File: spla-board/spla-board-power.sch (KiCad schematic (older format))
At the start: 70 parts, among them J12 J_POWER, J4 J_POWER2, J7 Barrel_Jack, U14 TLV73311PDBV, U7 ST1S10PHR, U8 ST1S10PHR, U9 TLV73325PDBV

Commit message: schematic/pcb: Remove unnecessary electrolytic capacitors.
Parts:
- removed C71: NOSTUFF, Capacitor_THT:CP_Radial_D10.0mm_P5.00mm, symbol Device:CP
- removed C72: NOSTUFF, Capacitor_THT:CP_Radial_D7.5mm_P2.50mm, symbol Device:CP
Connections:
- wire segments 244 -> 237
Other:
- moved on the sheet: J7, TP6
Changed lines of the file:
@@
 L Connector:Barrel_Jack J7
 U 1 1 5E532515
-P 1050 3450
-F 0 "J7" H 1107 3775 50  0000 C CNN
-F 1 "Barrel_Jack" H 1107 3684 50  0000 C CNN
-F 2 "Connector_BarrelJack:BarrelJack_CUI_PJ-036AH-SMT_Horizontal" H 1100 3410 50  0001 C CNN
-F 3 "~" H 1100 3410 50  0001 C CNN
-F 4 "CP-036AHPJCT-ND" H 1050 3450 50  0001 C CNN "Digikey"
-F 5 "PJ-036AH-SMT-TR" H 1050 3450 50  0001 C CNN "Manufacturer Id"
-F 6 "CUI Devices" H 1050 3450 50  0001 C CNN "Manufacturer"
-	1    1050 3450
-	1    0    0    -1
-$EndComp
-Wire Wire Line
-	1350 3550 1450 3550
-Wire Wire Line
-	1350 3350 1450 3350
-Wire Wire Line
-	1450 3350 1450 3250
+P 1600 3450
+F 0 "J7" H 1657 3775 50  0000 C CNN
+F 1 "Barrel_Jack" H 1657 3684 50  0000 C CNN
+F 2 "Connector_BarrelJack:BarrelJack_CUI_PJ-036AH-SMT_Horizontal" H 1650 3410 50  0001 C CNN
+F 3 "~" H 1650 3410 50  0001 C CNN
+F 4 "CP-036AHPJCT-ND" H 1600 3450 50  0001 C CNN "Digikey"
+F 5 "PJ-036AH-SMT-TR" H 1600 3450 50  0001 C CNN "Manufacturer Id"
+F 6 "CUI Devices" H 1600 3450 50  0001 C CNN "Manufacturer"
+	1    1600 3450
+	1    0    0    -1
+$EndComp
+Wire Wire Line
+	1900 3550 2000 3550
 $Comp
 L power:+12V #PWR029
 U 1 1 5E534EED
-P 1450 3250
-F 0 "#PWR029" H 1450 3100 50  0001 C CNN
-F 1 "+12V" H 1465 3423 50  0000 C CNN
-F 2 "" H 1450 3250 50  0001 C CNN
-F 3 "" H 1450 3250 50  0001 C CNN
-	1    1450 3250
-	1    0    0    -1
-$EndComp
-Wire Wire Line
-	1450 3350 1750 3350
-Connection ~ 1450 3350
+P 3400 3200
+F 0 "#PWR029" H 3400 3050 50  0001 C CNN
+F 1 "+12V" H 3415 3373 50  0000 C CNN
+F 2 "" H 3400 3200 50  0001 C CNN
+F 3 "" H 3400 3200 50  0001 C CNN
+	1    3400 3200
+	1    0    0    -1
+$EndComp
 $Comp
 L power:+5V #PWR041
@@
 L power:PWR_FLAG #FLG0101
 U 1 1 5F9445F5
-P 2050 3350
-F 0 "#FLG0101" H 2050 3425 50  0001 C CNN
-F 1 "PWR_FLAG" H 2050 3523 50  0000 C CNN
-F 2 "" H 2050 3350 50  0001 C CNN
-F 3 "~" H 2050 3350 50  0001 C CNN
-	1    2050 3350
+P 2450 3350
+F 0 "#FLG0101" H 2450 3425 50  0001 C CNN
+F 1 "PWR_FLAG" H 2450 3523 50  0000 C CNN
+F 2 "" H 2450 3350 50  0001 C CNN
+F 3 "~" H 2450 3350 50  0001 C CNN
+	1    2450 3350
 	1    0    0    -1
 $EndComp
@@
 Text Notes 5000 4400 2    50   ~ 0
 SYNC = use internal 900kHz oscillator
-Connection ~ 2050 3350
-Wire Wire Line
-	2050 3350 2400 3350
+Connection ~ 2450 3350
 $Comp
 L Device:R_Small R87
@@
 	4100 10250 4100 10350
 Connection ~ 2850 4050
-Wire Wire Line
-	2850 4050 2400 4050
 $Comp
 L Connector:TestPoint TP6
 U 1 1 5EAFCBB1
-P 2850 4050
-F 0 "TP6" H 2908 4168 50  0000 L CNN
-F 1 "TP_GND" H 2908 4077 50  0000 L CNN
-F 2 "TestPoint:TestPoint_Pad_D2.0mm" H 3050 4050 50  0001 C CNN
-F 3 "~" H 3050 4050 50  0001 C CNN
-F 4 "N/A" H 2850 4050 50  0001 C CNN "Digikey"
-F 5 "N/A" H 2850 4050 50  0001 C CNN "Manufacturer Id"
-F 6 "N/A" H 2850 4050 50  0001 C CNN "Manufacturer"
-	1    2850 4050
-	1    0    0    -1
-$EndComp
-Wire Wire Line
-	1450 3550 1450 4050
+P 2850 3950
+F 0 "TP6" H 2908 4068 50  0000 L CNN
+F 1 "TP_GND" H 2908 3977 50  0000 L CNN
+F 2 "TestPoint:TestPoint_Pad_D2.0mm" H 3050 3950 50  0001 C CNN
+F 3 "~" H 3050 3950 50  0001 C CNN
+F 4 "N/A" H 2850 3950 50  0001 C CNN "Digikey"
+F 5 "N/A" H 2850 3950 50  0001 C CNN "Manufacturer Id"
+F 6 "N/A" H 2850 3950 50  0001 C CNN "Manufacturer"
+	1    2850 3950
+	1    0    0    -1
+$EndComp
+Wire Wire Line
+	2000 3550 2000 4050
 $Comp
 L SPLA:BomExtra BOM?
@@
 L power:GND #PWR030
 U 1 1 5E5334D6
-P 2850 4050
-F 0 "#PWR030" H 2850 3800 50  0001 C CNN
-F 1 "GND" H 2855 3877 50  0000 C CNN
-F 2 "" H 2850 4050 50  0001 C CNN
-F 3 "" H 2850 4050 50  0001 C CNN
-	1    2850 4050
-	1    0    0    -1
-$EndComp
-$Comp
-L Device:CP C71
-U 1 1 5EE4A2E3
-P 1750 3700
-F 0 "C71" H 1868 3746 50  0000 L CNN
-F 1 "NOSTUFF" H 1868 3655 50  0000 L CNN
-F 2 "Capacitor_THT:CP_Radial_D10.0mm_P5.00mm" H 1788 3550 50  0001 C CNN
-F 3 "~" H 1750 3700 50  0001 C CNN
-F 4 "N/A" H 1750 3700 50  0001 C CNN "Digikey"
-F 5 "N/A" H 1750 3700 50  0001 C CNN "Manufacturer"
-F 6 "N/A" H 1750 3700 50  0001 C CNN "Manufacturer Id"
-	1    1750 3700
-	1    0    0    -1
-$EndComp
-$Comp
-L Device:CP C72
-U 1 1 5EE4A640
-P 2400 3700
-F 0 "C72" H 2518 3746 50  0000 L CNN
-F 1 "NOSTUFF" H 2518 3655 50  0000 L CNN
-F 2 "Capacitor_THT:CP_Radial_D7.5mm_P2.50mm" H 2438 3550 50  0001 C CNN
-F 3 "~" H 2400 3700 50  0001 C CNN
-F 4 "N/A" H 2400 3700 50  0001 C CNN "Digikey"
-F 5 "N/A" H 2400 3700 50  0001 C CNN "Manufacturer"
-F 6 "N/A" H 2400 3700 50  0001 C CNN "Manufacturer Id"
-	1    2400 3700
-	1    0    0    -1
-$EndComp
-Wire Wire Line
-	1750 3550 1750 3350
-Connection ~ 1750 3350
-Wire Wire Line
-	1750 3350 2050 3350
-Wire Wire Line
-	1750 3850 1750 4050
-Connection ~ 1750 4050
-Wire Wire Line
-	1750 4050 1450 4050
-Wire Wire Line
-	2400 3850 2400 4050
-Connection ~ 2400 4050
-Wire Wire Line
-	2400 4050 1750 4050
-Wire Wire Line
-	2400 3550 2400 3350
-Connection ~ 2400 3350
-Wire Wire Line
-	2400 3350 2850 3350
+P 2850 4150
+F 0 "#PWR030" H 2850 3900 50  0001 C CNN
+F 1 "GND" H 2855 3977 50  0000 C CNN
+F 2 "" H 2850 4150 50  0001 C CNN
+F 3 "" H 2850 4150 50  0001 C CNN
+	1    2850 4150
+	1    0    0    -1
+$EndComp
+Wire Wire Line
+	2450 3350 2850 3350
+Wire Wire Line
+	2000 4050 2850 4050
+Wire Wire Line
+	2850 3950 2850 4050
+Wire Wire Line
+	2850 4050 2850 4150
+Wire Wire Line
+	3400 3200 3400 3350
+Wire Wire Line
+	1900 3350 2450 3350
 $EndSCHEMATC

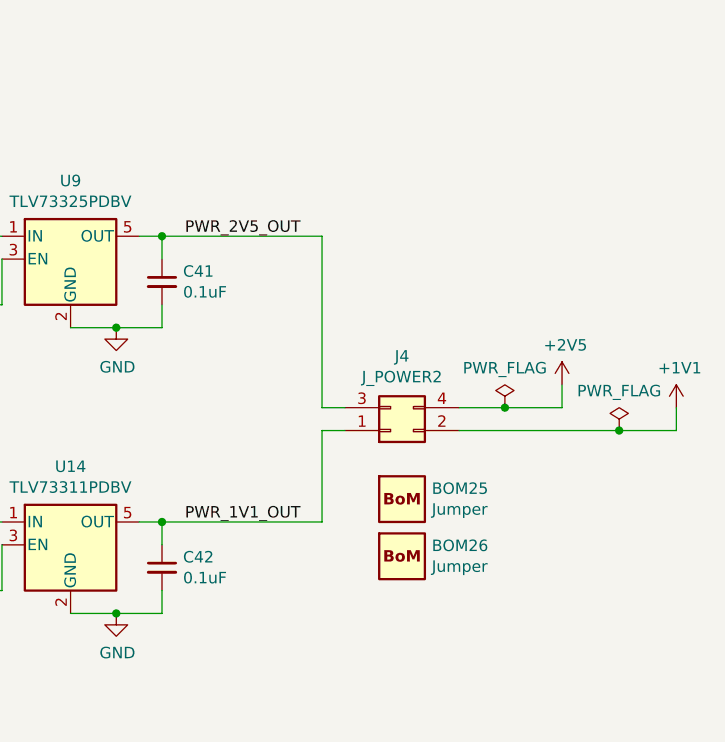
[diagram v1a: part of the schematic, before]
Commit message: schematic/pcb: Remove J4, which is unnecessary and meltable.
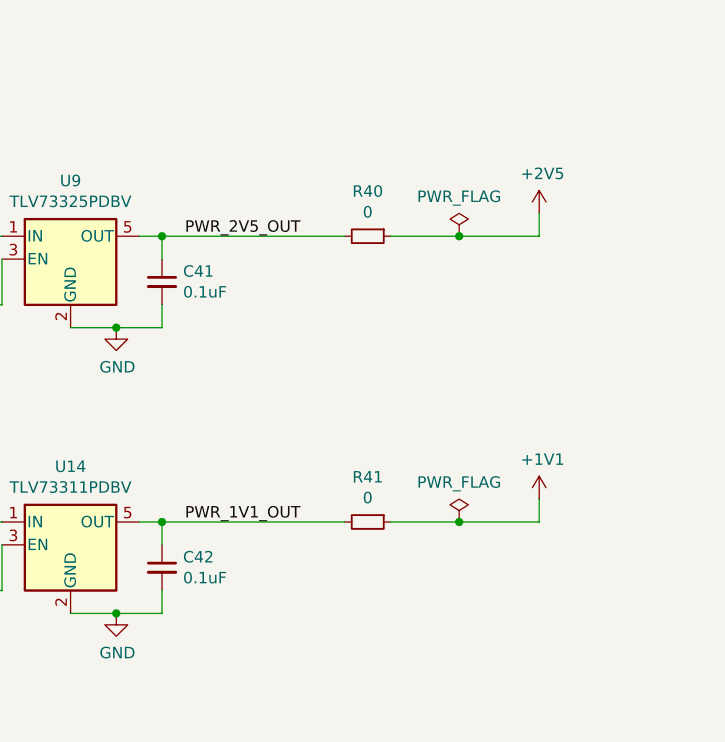
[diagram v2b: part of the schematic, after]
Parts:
- removed BOM25, BOM26: Jumper, SPLA:BoM, symbol SPLA:BomExtra
- removed J4: J_POWER2, Connector_PinHeader_2.54mm:PinHeader_2x02_P2.54mm_Vertical, symbol Connector_Generic:Conn_02x02_Odd_Even
- added R40, R41: 0, Resistor_SMD:R_0603_1608Metric, symbol Device:R_Small
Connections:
- net +1V1: now also R41.1
- net +2V5: now also R40.1
- net PWR_1V1_OUT: now also R41.2
- net PWR_2V5_OUT: now also R40.2
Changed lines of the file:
@@
 Connection ~ 12050 5100
 Wire Wire Line
-	15350 5850 15350 5750
-Wire Wire Line
-	15850 5850 15850 5950
+	15250 5100 15250 5000
+Wire Wire Line
+	15250 6250 15250 6350
 $Comp
 L power:+1V1 #PWR044
 U 1 1 5E56FFF6
-P 15850 5850
-F 0 "#PWR044" H 15850 5700 50  0001 C CNN
-F 1 "+1V1" H 15865 6023 50  0000 C CNN
-F 2 "" H 15850 5850 50  0001 C CNN
-F 3 "" H 15850 5850 50  0001 C CNN
-	1    15850 5850
+P 15250 6250
+F 0 "#PWR044" H 15250 6100 50  0001 C CNN
+F 1 "+1V1" H 15265 6423 50  0000 C CNN
+F 2 "" H 15250 6250 50  0001 C CNN
+F 3 "" H 15250 6250 50  0001 C CNN
+	1    15250 6250
 	1    0    0    -1
 $EndComp
@@
 L power:+2V5 #PWR043
 U 1 1 5E56BE1E
-P 15350 5750
-F 0 "#PWR043" H 15350 5600 50  0001 C CNN
-F 1 "+2V5" H 15365 5923 50  0000 C CNN
-F 2 "" H 15350 5750 50  0001 C CNN
-F 3 "" H 15350 5750 50  0001 C CNN
-	1    15350 5750
+P 15250 5000
+F 0 "#PWR043" H 15250 4850 50  0001 C CNN
+F 1 "+2V5" H 15265 5173 50  0000 C CNN
+F 2 "" H 15250 5000 50  0001 C CNN
+F 3 "" H 15250 5000 50  0001 C CNN
+	1    15250 5000
 	1    0    0    -1
 $EndComp
@@
 Wire Wire Line
 	11850 6350 12050 6350
-$Comp
-L Connector_Generic:Conn_02x02_Odd_Even J4
-U 1 1 5F14B7D8
-P 14600 5950
-F 0 "J4" H 14650 5625 50  0000 C CNN
-F 1 "J_POWER2" H 14650 5716 50  0000 C CNN
-F 2 "Connector_PinHeader_2.54mm:PinHeader_2x02_P2.54mm_Vertical" H 14600 5950 50  0001 C CNN
-F 3 "~" H 14600 5950 50  0001 C CNN
-F 4 "S2011EC-40-ND" H 14600 5950 50  0001 C CNN "Digikey"
-F 5 "PRPC040DAAN-RC" H 14600 5950 50  0001 C CNN "Manufacturer Id"
-F 6 "Sullins Connector Solutions" H 14600 5950 50  0001 C CNN "Manufacturer"
-	1    14600 5950
-	1    0    0    1
-$EndComp
-Wire Wire Line
-	13600 5100 14300 5100
-Wire Wire Line
-	14300 5100 14300 5850
-Wire Wire Line
-	14300 5850 14400 5850
 Connection ~ 13600 5100
-Wire Wire Line
-	14400 5950 14300 5950
-Wire Wire Line
-	14300 5950 14300 6350
-Wire Wire Line
-	14300 6350 13600 6350
 Connection ~ 13600 6350
 $Comp
 L power:PWR_FLAG #FLG0106
 U 1 1 5F180F83
-P 15100 5850
-F 0 "#FLG0106" H 15100 5925 50  0001 C CNN
-F 1 "PWR_FLAG" H 15100 6023 50  0000 C CNN
-F 2 "" H 15100 5850 50  0001 C CNN
-F 3 "~" H 15100 5850 50  0001 C CNN
-	1    15100 5850
+P 14900 5100
+F 0 "#FLG0106" H 14900 5175 50  0001 C CNN
+F 1 "PWR_FLAG" H 14900 5273 50  0000 C CNN
+F 2 "" H 14900 5100 50  0001 C CNN
+F 3 "~" H 14900 5100 50  0001 C CNN
+	1    14900 5100
 	1    0    0    -1
 $EndComp
@@
 L power:PWR_FLAG #FLG0107
 U 1 1 5F1887AE
-P 15600 5950
-F 0 "#FLG0107" H 15600 6025 50  0001 C CNN
-F 1 "PWR_FLAG" H 15600 6123 50  0000 C CNN
-F 2 "" H 15600 5950 50  0001 C CNN
-F 3 "~" H 15600 5950 50  0001 C CNN
-	1    15600 5950
-	1    0    0    -1
-$EndComp
-Wire Wire Line
-	15350 5850 15100 5850
-Connection ~ 15100 5850
-Wire Wire Line
-	15100 5850 14900 5850
-Wire Wire Line
-	14900 5950 15600 5950
-Connection ~ 15600 5950
-Wire Wire Line
-	15600 5950 15850 5950
+P 14900 6350
+F 0 "#FLG0107" H 14900 6425 50  0001 C CNN
+F 1 "PWR_FLAG" H 14900 6523 50  0000 C CNN
+F 2 "" H 14900 6350 50  0001 C CNN
+F 3 "~" H 14900 6350 50  0001 C CNN
+	1    14900 6350
+	1    0    0    -1
+$EndComp
 Text Label 13700 5100 0    50   ~ 0
 PWR_2V5_OUT
@@
 $Comp
 L SPLA:BomExtra BOM?
-U 1 1 5EC1E4A3
-P 14650 6250
-AR Path="/5E50E589/5EC1E4A3" Ref="BOM?"  Part="1"
-AR Path="/5E50D39B/5EC1E4A3" Ref="BOM25"  Part="1"
-F 0 "BOM25" H 14780 6296 50  0000 L CNN
-F 1 "Jumper" H 14780 6205 50  0000 L CNN
-F 2 "SPLA:BoM" H 14650 6250 50  0001 C CNN
-F 3 "" H 14650 6250 50  0001 C CNN
-F 4 "S9337-ND" H 14650 6250 50  0001 C CNN "Digikey"
-F 5 "QPC02SXGN-RC" H 14650 6250 50  0001 C CNN "Manufacturer Id"
-F 6 "Sullins Connector Solutions" H 14650 6250 50  0001 C CNN "Manufacturer"
-	1    14650 6250
-	1    0    0    -1
-$EndComp
-$Comp
-L SPLA:BomExtra BOM?
-U 1 1 5EC2D1EF
-P 14650 6500
-AR Path="/5E50E589/5EC2D1EF" Ref="BOM?"  Part="1"
-AR Path="/5E50D39B/5EC2D1EF" Ref="BOM26"  Part="1"
-F 0 "BOM26" H 14780 6546 50  0000 L CNN
-F 1 "Jumper" H 14780 6455 50  0000 L CNN
-F 2 "SPLA:BoM" H 14650 6500 50  0001 C CNN
-F 3 "" H 14650 6500 50  0001 C CNN
-F 4 "S9337-ND" H 14650 6500 50  0001 C CNN "Digikey"
-F 5 "QPC02SXGN-RC" H 14650 6500 50  0001 C CNN "Manufacturer Id"
-F 6 "Sullins Connector Solutions" H 14650 6500 50  0001 C CNN "Manufacturer"
-	1    14650 6500
-	1    0    0    -1
-$EndComp
-$Comp
-L SPLA:BomExtra BOM?
 U 1 1 5EC3BD64
 P 10700 5900
@@
 Wire Wire Line
 	1900 3350 2450 3350
+$Comp
+L Device:R_Small R40
+U 1 1 5FB785AC
+P 14500 5100
+F 0 "R40" V 14304 5100 50  0000 C CNN
+F 1 "0" V 14395 5100 50  0000 C CNN
+F 2 "Resistor_SMD:R_0603_1608Metric" H 14500 5100 50  0001 C CNN
+F 3 "~" H 14500 5100 50  0001 C CNN
+F 4 "2019-RK73Z1JTTDCT-ND" H 14500 5100 50  0001 C CNN "Digikey"
+F 5 "KOA Speer Electronics Inc." H 14500 5100 50  0001 C CNN "Manufacturer"
+F 6 "RK73Z1JTTD" H 14500 5100 50  0001 C CNN "Manufacturer Id"
+	1    14500 5100
+	0    1    1    0
+$EndComp
+$Comp
+L Device:R_Small R41
+U 1 1 5FB7903C
+P 14500 6350
+F 0 "R41" V 14304 6350 50  0000 C CNN
+F 1 "0" V 14395 6350 50  0000 C CNN
+F 2 "Resistor_SMD:R_0603_1608Metric" H 14500 6350 50  0001 C CNN
+F 3 "~" H 14500 6350 50  0001 C CNN
+F 4 "2019-RK73Z1JTTDCT-ND" H 14500 6350 50  0001 C CNN "Digikey"
+F 5 "KOA Speer Electronics Inc." H 14500 6350 50  0001 C CNN "Manufacturer"
+F 6 "RK73Z1JTTD" H 14500 6350 50  0001 C CNN "Manufacturer Id"
+	1    14500 6350
+	0    1    1    0
+$EndComp
+Wire Wire Line
+	13600 5100 14400 5100
+Wire Wire Line
+	14600 5100 14900 5100
+Wire Wire Line
+	14900 6350 14600 6350
+Wire Wire Line
+	13600 6350 14400 6350
+Wire Wire Line
+	14900 5100 15250 5100
+Connection ~ 14900 5100
+Wire Wire Line
+	14900 6350 15250 6350
+Connection ~ 14900 6350
 $EndSCHEMATC

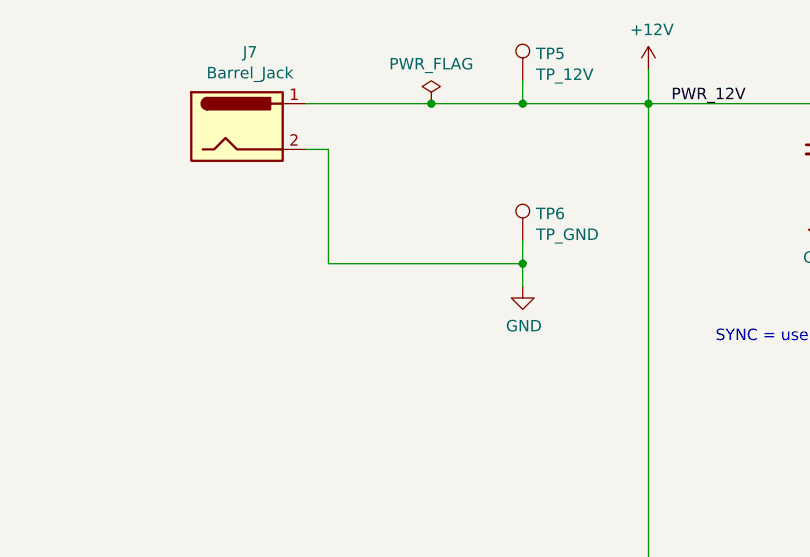
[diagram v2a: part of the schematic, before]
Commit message: schematic/pcb: Add discrete power switch.
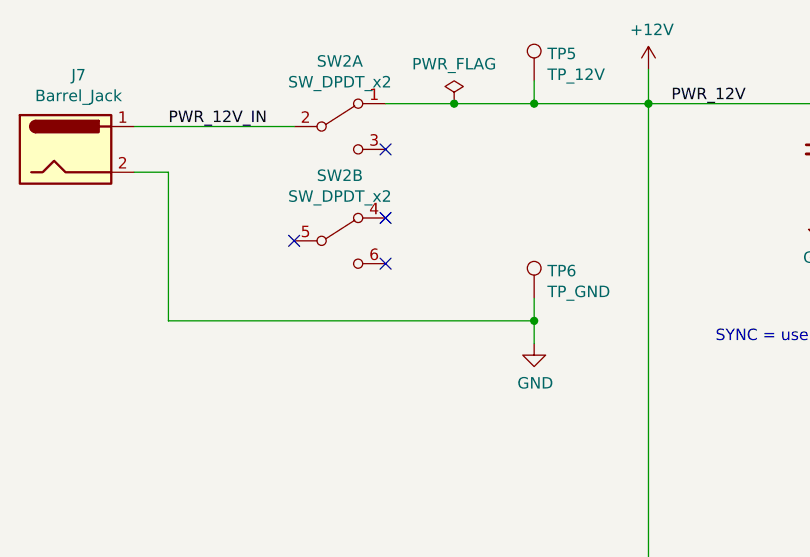
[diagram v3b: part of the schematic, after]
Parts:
- added SW2: SW_DPDT_x2, SPLA:JS202011SCQN, symbol Switch:SW_DPDT_x2
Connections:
- net +12V: now also SW2.1 (A); no longer J7.1
- new net PWR_12V_IN: J7.1, SW2.2 (B)
- no-connect marks 0 -> 4
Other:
- moved on the sheet: J7, TP5, TP6
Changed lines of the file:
@@
 L Connector:Barrel_Jack J7
 U 1 1 5E532515
-P 1600 3450
-F 0 "J7" H 1657 3775 50  0000 C CNN
-F 1 "Barrel_Jack" H 1657 3684 50  0000 C CNN
-F 2 "Connector_BarrelJack:BarrelJack_CUI_PJ-036AH-SMT_Horizontal" H 1650 3410 50  0001 C CNN
-F 3 "~" H 1650 3410 50  0001 C CNN
-F 4 "CP-036AHPJCT-ND" H 1600 3450 50  0001 C CNN "Digikey"
-F 5 "PJ-036AH-SMT-TR" H 1600 3450 50  0001 C CNN "Manufacturer Id"
-F 6 "CUI Devices" H 1600 3450 50  0001 C CNN "Manufacturer"
-	1    1600 3450
-	1    0    0    -1
-$EndComp
-Wire Wire Line
-	1900 3550 2000 3550
+P 850 3550
+F 0 "J7" H 907 3875 50  0000 C CNN
+F 1 "Barrel_Jack" H 907 3784 50  0000 C CNN
+F 2 "Connector_BarrelJack:BarrelJack_CUI_PJ-036AH-SMT_Horizontal" H 900 3510 50  0001 C CNN
+F 3 "~" H 900 3510 50  0001 C CNN
+F 4 "CP-036AHPJCT-ND" H 850 3550 50  0001 C CNN "Digikey"
+F 5 "PJ-036AH-SMT-TR" H 850 3550 50  0001 C CNN "Manufacturer Id"
+F 6 "CUI Devices" H 850 3550 50  0001 C CNN "Manufacturer"
+	1    850  3550
+	1    0    0    -1
+$EndComp
 $Comp
 L power:+12V #PWR029
@@
 L Connector:TestPoint TP5
 U 1 1 5E6077CA
-P 2850 3250
-F 0 "TP5" H 2908 3368 50  0000 L CNN
-F 1 "TP_12V" H 2908 3277 50  0000 L CNN
-F 2 "TestPoint:TestPoint_Pad_D2.0mm" H 3050 3250 50  0001 C CNN
-F 3 "~" H 3050 3250 50  0001 C CNN
-F 4 "N/A" H 2850 3250 50  0001 C CNN "Digikey"
-F 5 "N/A" H 2850 3250 50  0001 C CNN "Manufacturer Id"
-F 6 "N/A" H 2850 3250 50  0001 C CNN "Manufacturer"
-	1    2850 3250
-	1    0    0    -1
-$EndComp
-Wire Wire Line
-	2850 3350 2850 3250
+P 2900 3250
+F 0 "TP5" H 2958 3368 50  0000 L CNN
+F 1 "TP_12V" H 2958 3277 50  0000 L CNN
+F 2 "TestPoint:TestPoint_Pad_D2.0mm" H 3100 3250 50  0001 C CNN
+F 3 "~" H 3100 3250 50  0001 C CNN
+F 4 "N/A" H 2900 3250 50  0001 C CNN "Digikey"
+F 5 "N/A" H 2900 3250 50  0001 C CNN "Manufacturer Id"
+F 6 "N/A" H 2900 3250 50  0001 C CNN "Manufacturer"
+	1    2900 3250
+	1    0    0    -1
+$EndComp
+Wire Wire Line
+	2900 3350 2900 3250
 $Comp
 L power:PWR_FLAG #FLG0101
 U 1 1 5F9445F5
-P 2450 3350
-F 0 "#FLG0101" H 2450 3425 50  0001 C CNN
-F 1 "PWR_FLAG" H 2450 3523 50  0000 C CNN
-F 2 "" H 2450 3350 50  0001 C CNN
-F 3 "~" H 2450 3350 50  0001 C CNN
-	1    2450 3350
+P 2550 3350
+F 0 "#FLG0101" H 2550 3425 50  0001 C CNN
+F 1 "PWR_FLAG" H 2550 3523 50  0000 C CNN
+F 2 "" H 2550 3350 50  0001 C CNN
+F 3 "~" H 2550 3350 50  0001 C CNN
+	1    2550 3350
 	1    0    0    -1
 $EndComp
@@
 Text Notes 5000 4400 2    50   ~ 0
 SYNC = use internal 900kHz oscillator
-Connection ~ 2450 3350
 $Comp
 L Device:R_Small R87
@@
 ~INH~ = Always On
 Wire Wire Line
-	2850 3350 3400 3350
-Connection ~ 2850 3350
+	2900 3350 3400 3350
 Wire Wire Line
 	4150 3850 4150 3750
@@
 Wire Wire Line
 	4100 10250 4100 10350
-Connection ~ 2850 4050
 $Comp
 L Connector:TestPoint TP6
 U 1 1 5EAFCBB1
-P 2850 3950
-F 0 "TP6" H 2908 4068 50  0000 L CNN
-F 1 "TP_GND" H 2908 3977 50  0000 L CNN
-F 2 "TestPoint:TestPoint_Pad_D2.0mm" H 3050 3950 50  0001 C CNN
-F 3 "~" H 3050 3950 50  0001 C CNN
-F 4 "N/A" H 2850 3950 50  0001 C CNN "Digikey"
-F 5 "N/A" H 2850 3950 50  0001 C CNN "Manufacturer Id"
-F 6 "N/A" H 2850 3950 50  0001 C CNN "Manufacturer"
-	1    2850 3950
-	1    0    0    -1
-$EndComp
-Wire Wire Line
-	2000 3550 2000 4050
+P 2900 4200
+F 0 "TP6" H 2958 4318 50  0000 L CNN
+F 1 "TP_GND" H 2958 4227 50  0000 L CNN
+F 2 "TestPoint:TestPoint_Pad_D2.0mm" H 3100 4200 50  0001 C CNN
+F 3 "~" H 3100 4200 50  0001 C CNN
+F 4 "N/A" H 2900 4200 50  0001 C CNN "Digikey"
+F 5 "N/A" H 2900 4200 50  0001 C CNN "Manufacturer Id"
+F 6 "N/A" H 2900 4200 50  0001 C CNN "Manufacturer"
+	1    2900 4200
+	1    0    0    -1
+$EndComp
 $Comp
 L SPLA:BomExtra BOM?
@@
 L power:GND #PWR030
 U 1 1 5E5334D6
-P 2850 4150
-F 0 "#PWR030" H 2850 3900 50  0001 C CNN
-F 1 "GND" H 2855 3977 50  0000 C CNN
-F 2 "" H 2850 4150 50  0001 C CNN
-F 3 "" H 2850 4150 50  0001 C CNN
-	1    2850 4150
-	1    0    0    -1
-$EndComp
-Wire Wire Line
-	2450 3350 2850 3350
-Wire Wire Line
-	2000 4050 2850 4050
-Wire Wire Line
-	2850 3950 2850 4050
-Wire Wire Line
-	2850 4050 2850 4150
+P 2900 4400
+F 0 "#PWR030" H 2900 4150 50  0001 C CNN
+F 1 "GND" H 2905 4227 50  0000 C CNN
+F 2 "" H 2900 4400 50  0001 C CNN
+F 3 "" H 2900 4400 50  0001 C CNN
+	1    2900 4400
+	1    0    0    -1
+$EndComp
 Wire Wire Line
 	3400 3200 3400 3350
-Wire Wire Line
-	1900 3350 2450 3350
 $Comp
 L Device:R_Small R40
@@
 	14900 6350 15250 6350
 Connection ~ 14900 6350
+$Comp
+L Switch:SW_DPDT_x2 SW2
+U 1 1 5F400F1C
+P 2050 3450
+F 0 "SW2" H 2050 3735 50  0000 C CNN
+F 1 "SW_DPDT_x2" H 2050 3644 50  0000 C CNN
+F 2 "SPLA:JS202011SCQN" H 2050 3450 50  0001 C CNN
+F 3 "https://ckswitches.com/media/1422/js.pdf" H 2050 3450 50  0001 C CNN
+F 4 "401-2002-1-ND" H 2050 3450 50  0001 C CNN "Digikey"
+F 5 "C&K" H 2050 3450 50  0001 C CNN "Manufacturer"
+F 6 "JS202011SCQN" H 2050 3450 50  0001 C CNN "Manufacturer Id"
+	1    2050 3450
+	1    0    0    -1
+$EndComp
+Wire Wire Line
+	1150 3450 1850 3450
+Text Label 1300 3450 0    50   ~ 0
+PWR_12V_IN
+Wire Wire Line
+	2250 3350 2550 3350
+Connection ~ 2900 3350
+Connection ~ 2550 3350
+Wire Wire Line
+	2550 3350 2900 3350
+Wire Wire Line
+	1150 3650 1300 3650
+$Comp
+L Switch:SW_DPDT_x2 SW2
+U 2 1 5F55178C
+P 2050 3950
+F 0 "SW2" H 2050 4235 50  0000 C CNN
+F 1 "SW_DPDT_x2" H 2050 4144 50  0000 C CNN
+F 2 "SPLA:JS202011SCQN" H 2050 3950 50  0001 C CNN
+F 3 "https://ckswitches.com/media/1422/js.pdf" H 2050 3950 50  0001 C CNN
+F 4 "401-2002-1-ND" H 2050 3950 50  0001 C CNN "Digikey"
+F 5 "C&K" H 2050 3950 50  0001 C CNN "Manufacturer"
+F 6 "JS202011SCQN" H 2050 3950 50  0001 C CNN "Manufacturer Id"
+	2    2050 3950
+	1    0    0    -1
+$EndComp
+Wire Wire Line
+	1300 3650 1300 4300
+Wire Wire Line
+	1300 4300 2900 4300
+NoConn ~ 2250 3850
+NoConn ~ 1850 3950
+Wire Wire Line
+	2900 4200 2900 4300
+Connection ~ 2900 4300
+Wire Wire Line
+	2900 4300 2900 4400
+NoConn ~ 2250 3550
+NoConn ~ 2250 4050
 $EndSCHEMATC
